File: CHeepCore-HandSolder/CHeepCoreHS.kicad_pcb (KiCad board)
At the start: 2 copper layers, 32 x 18.3 mm, 17 parts, among them J101 Conn_01x10, J102 Conn_01x10, J201 Conn_01x03, J301 USB_C_Receptacle_USB2.0_16P, U101 CH32V003FxPx, U301 3V3 LDO, Y101 Crystal_GND24

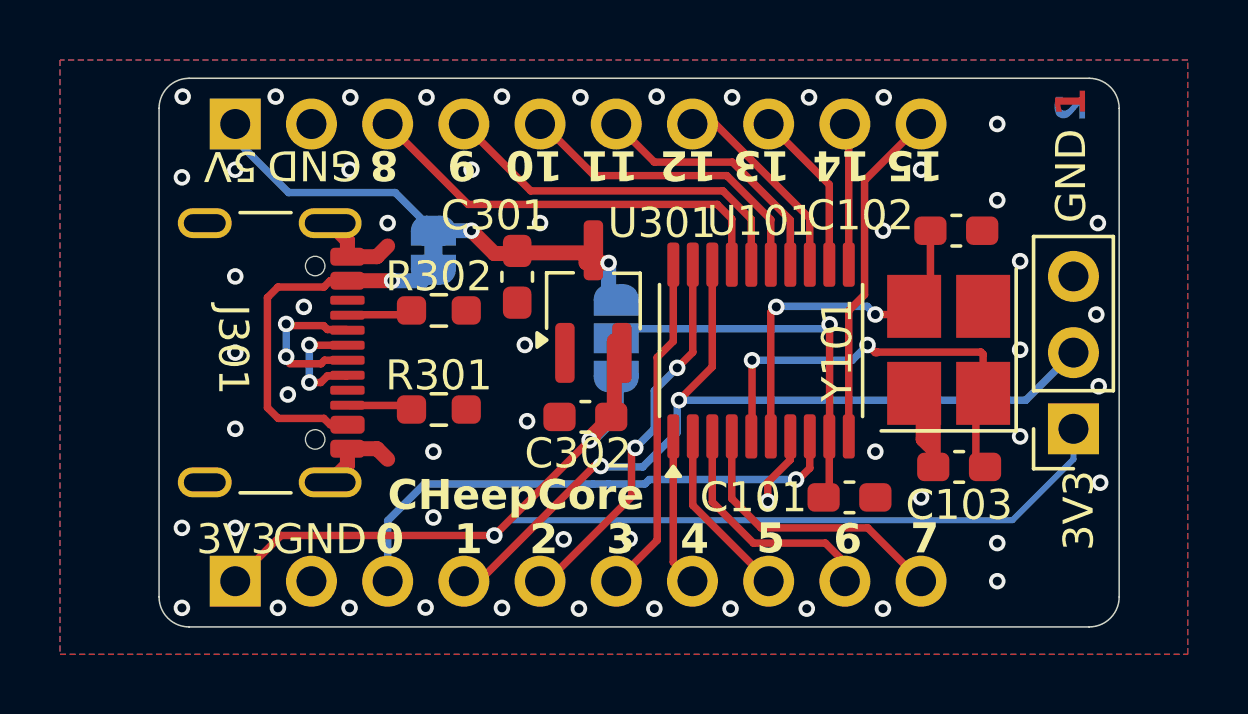
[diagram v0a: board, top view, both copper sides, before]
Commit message: Added teardrops
Added teardrops for better stability
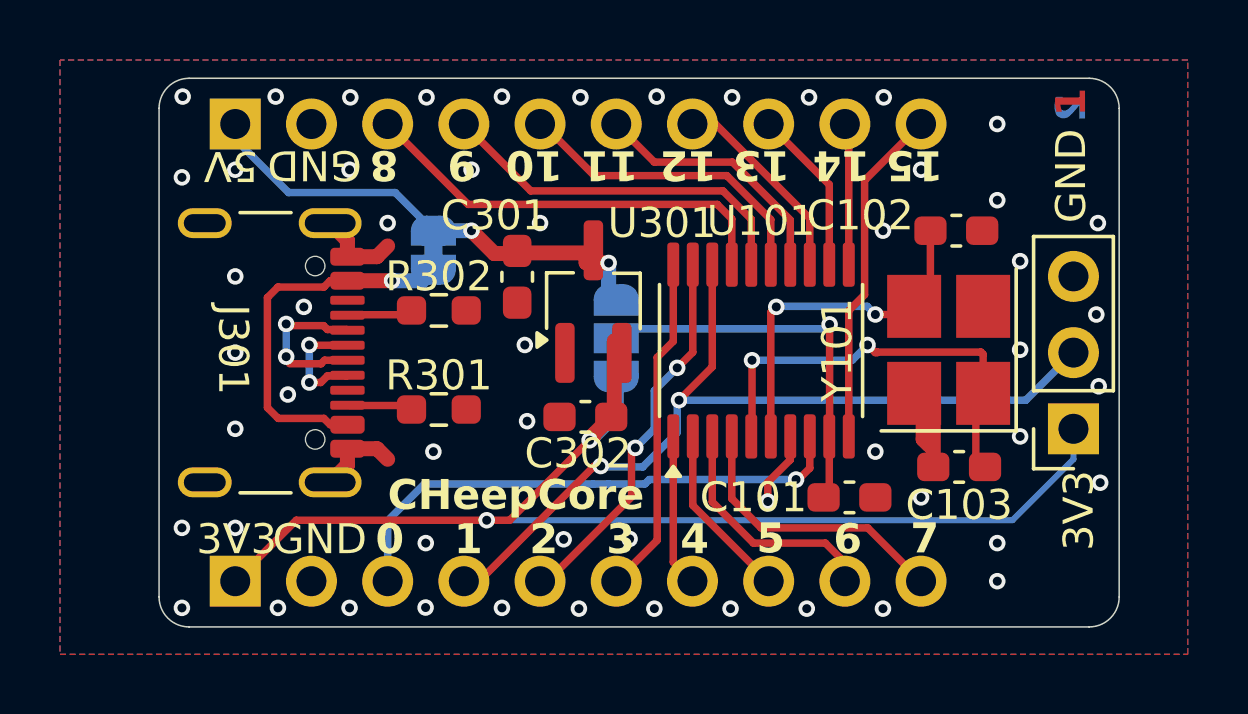
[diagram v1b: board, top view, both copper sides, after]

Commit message: Add USB smd pads on the back
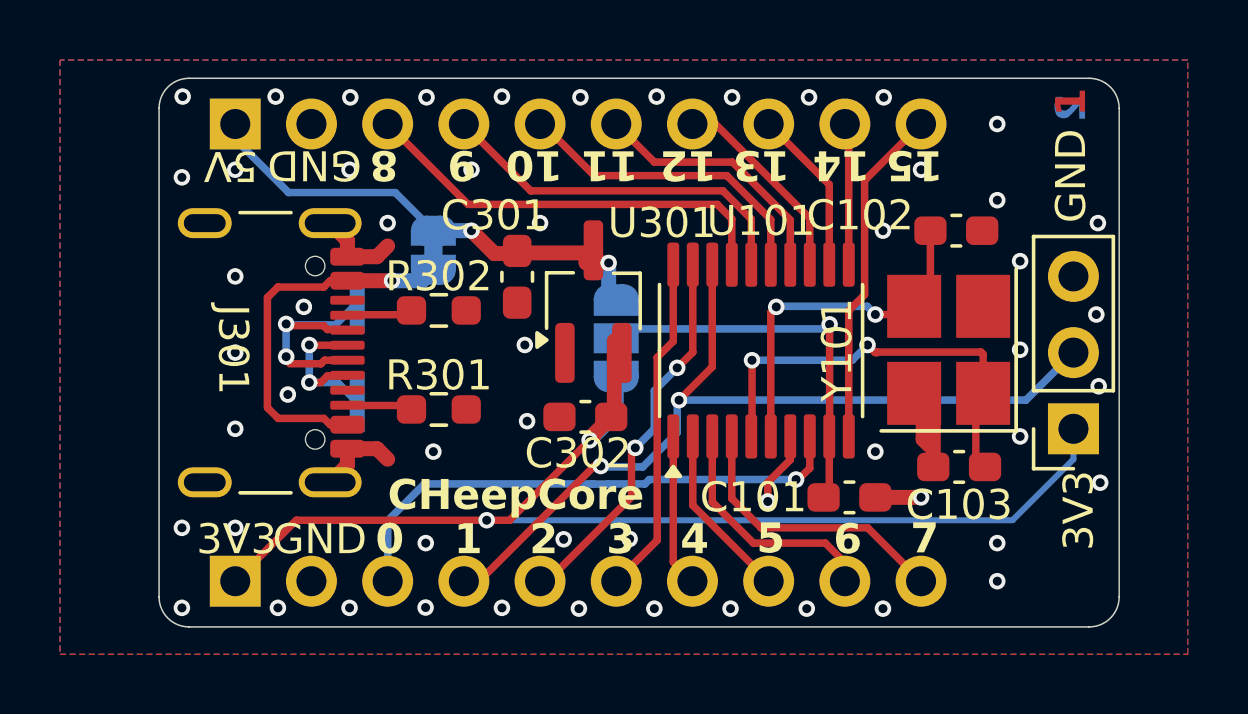
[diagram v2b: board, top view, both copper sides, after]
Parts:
- added J103: USB, Connector_PinHeader_1.00mm:PinHeader_2x01_P1.00mm_Vertical_SMD, B.Cu at (27.2, 31.2)
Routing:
- net /USB with LDO/D-: track 5.28 -> 7.96 mm
- net /USB with LDO/D+: track 3.89 -> 5.76 mm
- net GND: track 13.3 -> 14.8 mm
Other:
- board text added: "D+"
- board text added: "D-"
- board text added: "v0.0.1c"
- board text removed: "v0.0.1b"
